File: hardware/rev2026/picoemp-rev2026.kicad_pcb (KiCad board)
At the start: 2 copper layers, 40 x 130 mm, 53 parts, among them J1 EDGE-SMA, J2 1x2_Pin_Header, J3 MKDS 1,5/2-5.08, J4 EDGE-SMA, P1 Header 7, P2 Header 2, P3 Header 4, Q1 LDA111STR, Q2 RGT16BM65DTL, Q3 AO3422, Q4 AO3422, SW1 KSC741J LFS, SW2 KSC741J LFS, SW3 TL3301AF160QJ, T1 ATB322524, T2 ATB322524, U1 SC0915, U2 74LVC1G17

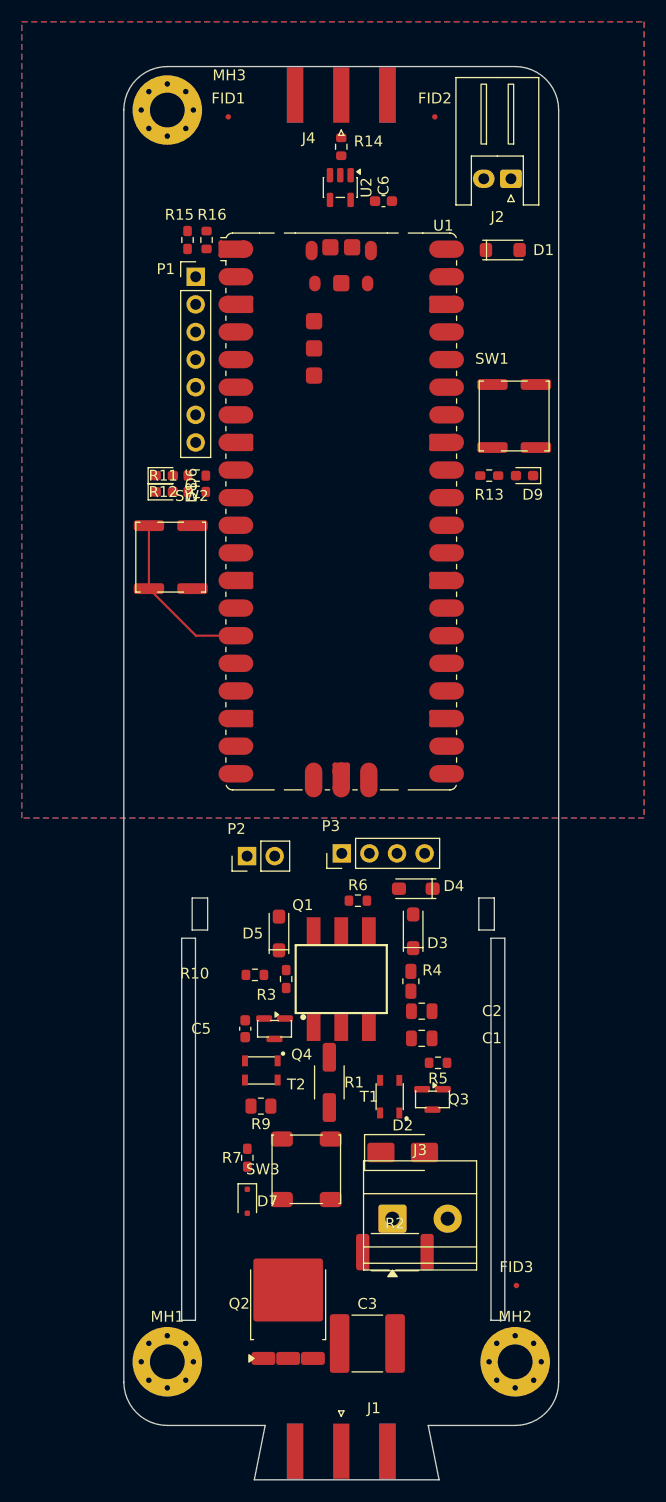
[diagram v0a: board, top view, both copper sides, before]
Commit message: Place fiducials clear of the HV section; J4 east-edge move blocked
Fiducials moved out of the old Altium scatter to three non-collinear spots,
all in the LOGIC half:
    FID1 (114.39, 23.872)   north-west
    FID2 (140.39, 41.000)   east, between D1 and SW1
    FID3 (108.39, 88.000)   west, below the Pico

None goes in the HV island or its side strips. A fiducial is unconnected
copper, and floating copper beside a 250 V section is exactly what was just
taken off the mounting holes in 0d4738f.

Worth stating plainly: with a hand build and no PCBA, these do nothing. They are
optical alignment targets for a pick-and-place machine. Placed as asked, but
deleting FID1-3 outright would be defensible.

J4 STAYS ON THE NORTH EDGE. The east-edge move was applied and then reverted:
Connector_Coaxial:SMA_Amphenol_132289_EdgeMount reports 4 shorting_items and
solder_mask_bridge violations between pad 1 (signal) and pad 2 (ground) at
rotations 0 and 180, and zero at 90 and -90. Measured across all four:

    rot    0 -> 4 violations
    rot   90 -> 0
    rot  180 -> 4
    rot  -90 -> 0

A rigid footprint cannot change whether its own pads overlap when you rotate it,
so one of the two readings is wrong. Rendering the footprint's F.Cu settles the
geometry: the three pads come out 5.080 x 1.500 mm on a 4.25 mm pitch, a clean
2.75 mm gap, no overlap. The pads are fine and the short is an artefact.

Which means the blocker is not the layout. But DRC is the fab gate, and shipping
the trigger connector in an orientation that trips a short I cannot account for
is worse than leaving it where it is. Note J1 -- the HV output SMA, on the same
footprint -- is at rot -90 and therefore in the clean set.

This also explains the pad-axis confusion behind the unresolved Q2 item: the
same (size a b) reading that makes these SMA pads overlap is what produces Q2's
0.080 mm. The two are one question, not two.

The USB collision is still real and unfixed: J4's courtyard spans x 118.81..129.97
on the no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
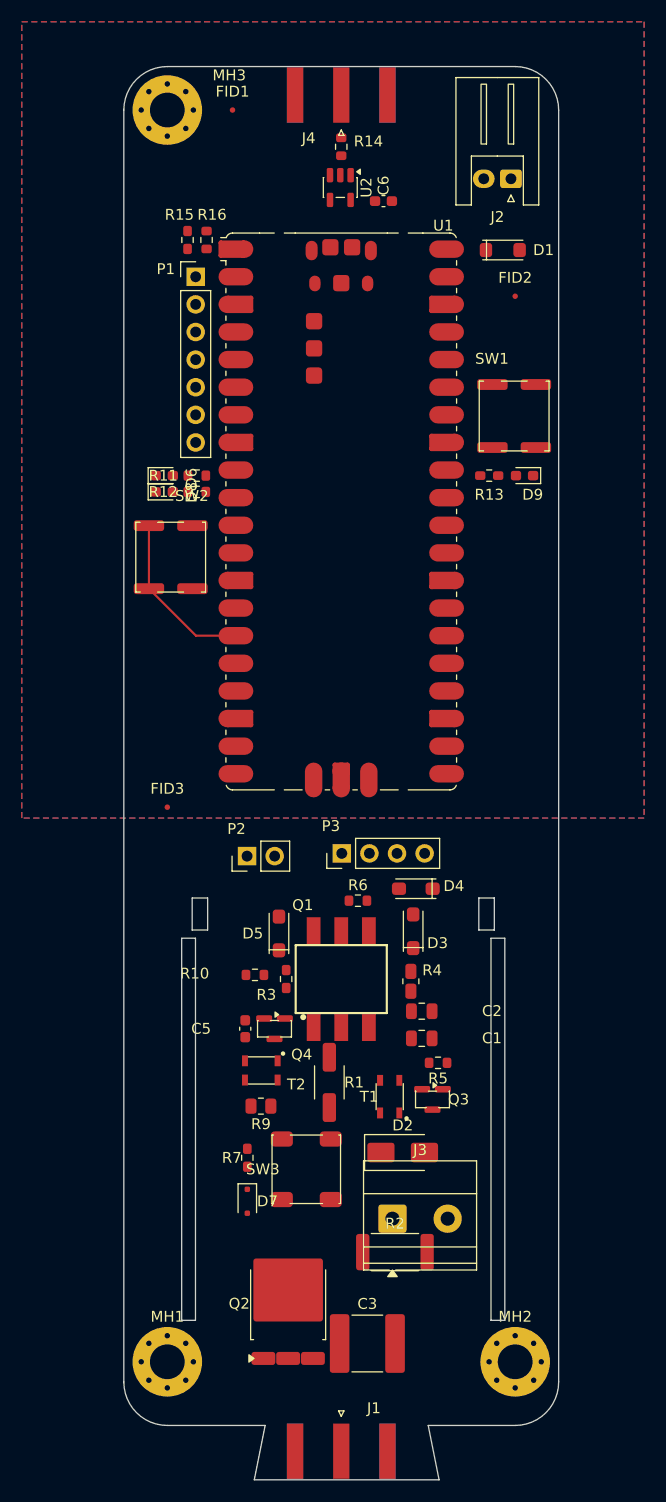
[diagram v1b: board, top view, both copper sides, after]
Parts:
- moved FID3 54.5 mm to (108.4, 88.0)
- moved FID2 18.1 mm to (140.4, 41.0)
- moved FID1 0.74 mm to (114.4, 23.9)
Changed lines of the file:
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@@
 	(footprint "Fiducial:Fiducial_0.5mm_Mask1.5mm"
 		(layer "F.Cu")
-		(at 140.5 132)
+		(at 108.39 88)
 		(descr "Fiducial, circular marking, 0.5mm bare copper, 1.5mm soldermask opening")
 		(tags "fiducial")
@@
 	(footprint "Fiducial:Fiducial_0.5mm_Mask1.5mm"
 		(layer "F.Cu")
-		(at 133 24.5)
+		(at 140.39 41)
 		(descr "Fiducial, circular marking, 0.5mm bare copper, 1.5mm soldermask opening")
 		(tags "fiducial")
@@
 	(footprint "Fiducial:Fiducial_0.5mm_Mask1.5mm"
 		(layer "F.Cu")
-		(at 114 24.5)
+		(at 114.39 23.872)
 		(descr "Fiducial, circular marking, 0.5mm bare copper, 1.5mm soldermask opening")
 		(tags "fiducial")

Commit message: Align MH1/MH2 with the bottom corners; correct the shield constraint claim
MH1/MH2 move 1.855 mm south to y=140.872, putting them 4.000 mm from the south
edge as well as 4.000 mm from the side edges. The R=4.000 corner arcs are
centred on exactly those points, so all three mounting holes now sit concentric
in their corners with a constant 2.400 mm FR4 web, instead of only MH3.

I previously said their Y was fixed by the Hammond 1551B shield and could not
move. That was inference from upstream's layout, not something I had checked,
and it was overstated. hardware/shield/picoempshield-1551BTRD-top.stl is
50 x 25 x 8 mm with corner bosses and contains no 32 mm screw pattern, so
nothing in the repo pins these holes to y=139.017.

What does matter is the 32.000 mm X spacing between MH1 and MH2 -- that is the
dimension a shield or bracket keys off. Only Y changed; a test now asserts the
spacing so a future corner tweak cannot quietly take it with it.

Since this rests on inference rather than a drawing, check the 1.855 mm shift
against the physical shield before ordering. If its screws are fixed relative to
the south edge, revert the Y and accept that the bottom corners are not
concentric.

Geometry checked: hole edges clear the shortened isolation slots by 4.07 mm and
the south board edge by 2.400 mm.

Test replaced with an all-holes version, plus the X-spacing guard: 68 -> 69.
DRC errors still 7, parity clean.

Co-Authored-By: Claude Opus 5 <noreply@anthropic.com>
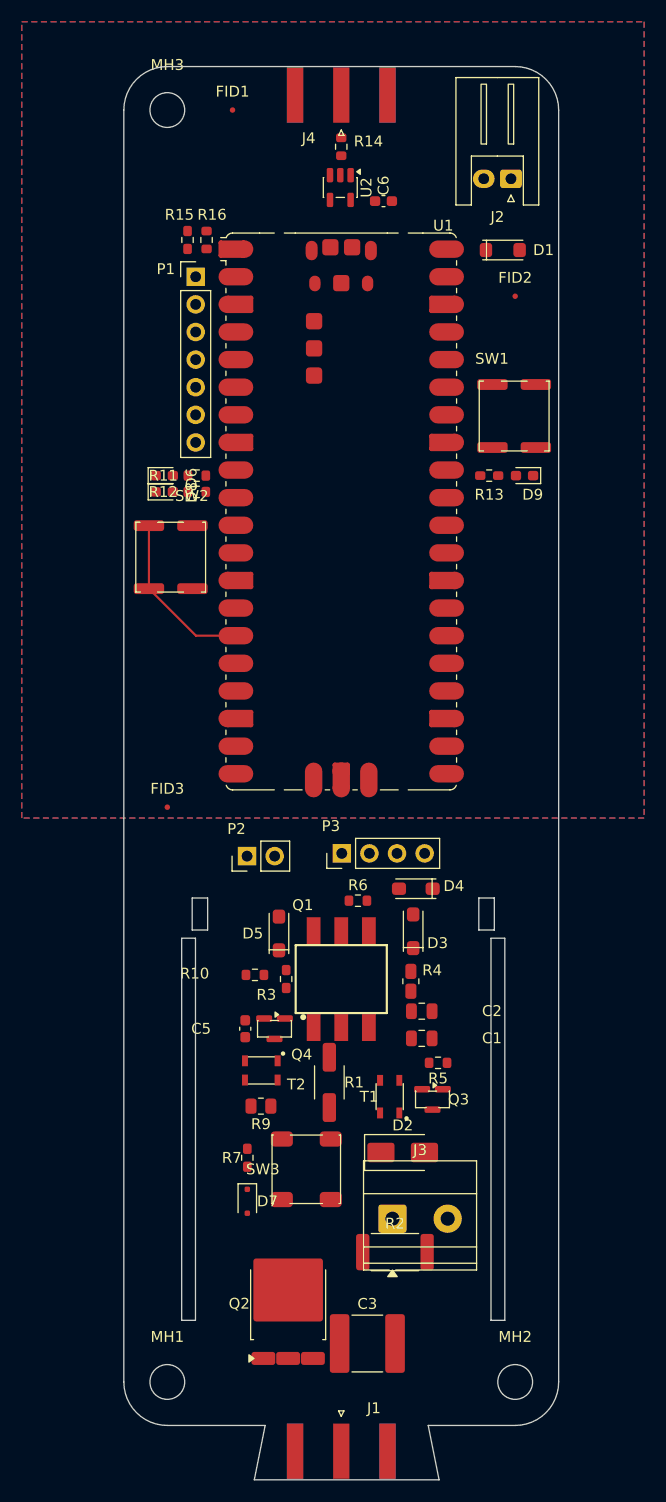
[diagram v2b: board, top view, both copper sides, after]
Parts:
- MH1, MH2, MH3: footprint MountingHole:MountingHole_3.2mm_M3_Pad_Via -> MountingHole:MountingHole_3.2mm_M3
- moved MH1 1.85 mm to (108.4, 140.9)
- moved MH2 1.85 mm to (140.4, 140.9)

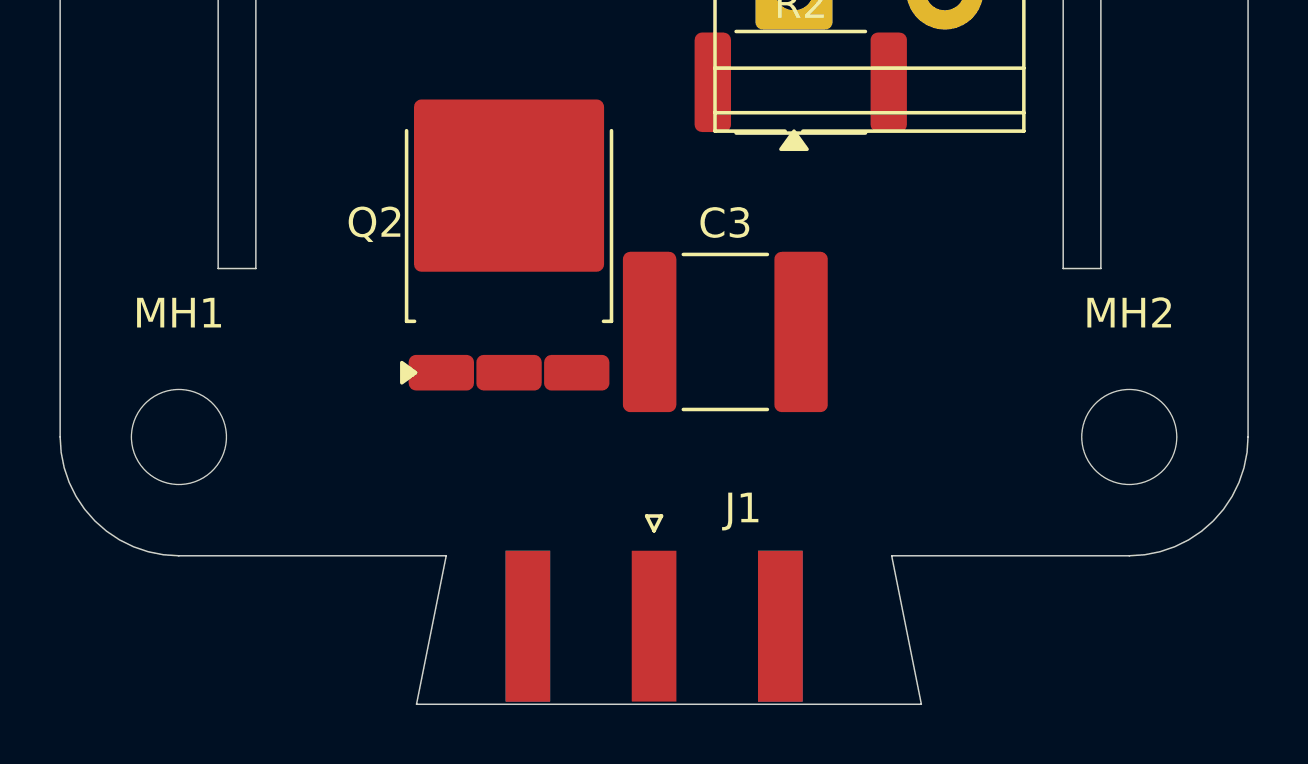
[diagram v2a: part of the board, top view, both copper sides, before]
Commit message: Centre the HV SMA tab; settle the pad-size axis question by plotting
The outcropping for J1 was drawn 0.500 mm east of the board centreline -- tab
centred on x=124.890 against a board centre of x=124.390. J1 itself sits at
x=124.390, so the connector was centred on the board but off-centre in its own
tab. Shifting the tab west by 0.500 mm centres both.

Separately, the pad-size axis question behind BOTH the Q2 0.080 mm item and the
J4 rotation short is now resolved, by plotting F.Cu and measuring the copper
that would actually reach the gerbers rather than reasoning about coordinates:

  J1 / J4 pads   1.500 mm wide, 4.250 mm pitch  -> 2.750 mm gaps.  Fine.
  Q2 lead pads   2.200 mm wide, 2.280 mm pitch  -> 0.080 mm gaps.  NOT fine.

So Q2's 0.080 mm is REAL, not a DRC artefact. The plot is the fabrication
output, and in it the three TO-252 lead pads are 2.200 mm across on a 2.286 mm
pitch. Those pads are HV_GATE, HV_OUT (collector) and HV_RTN (emitter). Holding
~250 V across 0.080 mm is close to the ~240 V that gap breaks down at in air,
and it is below JLCPCB's 0.127 mm minimum besides. Q2 needs a corrected
footprint before this board is ordered. Leaving the violation visible rather
than excluding it was the right call.

The same measurement explains J4: its pads only clear at rotations 90 and -90.
At 0 and 180 the plotted copper genuinely overlaps, so the east-edge placement
the user asked for cannot use this footprint as drawn. J1 is at -90 and is
clean.

Tests 69 -> 70.

Co-Authored-By: Claude Opus 5 <noreply@anthropic.com>
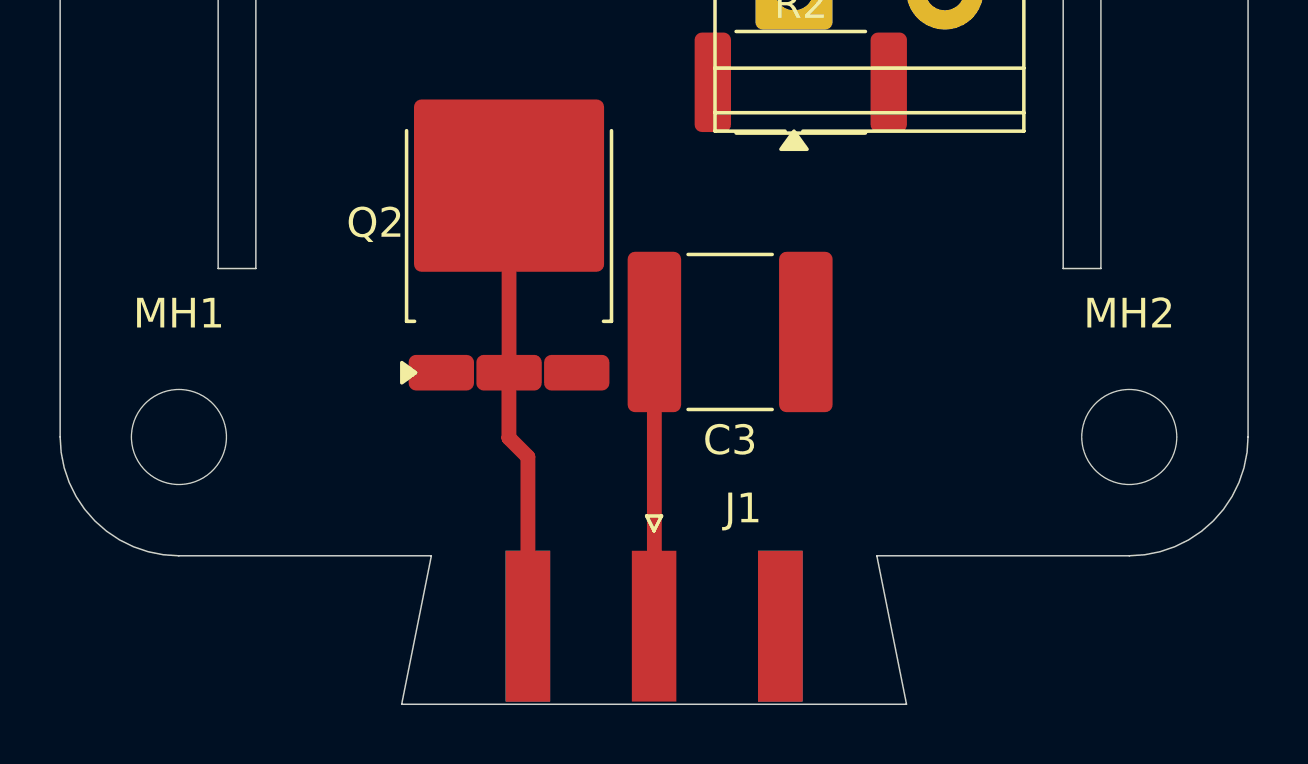
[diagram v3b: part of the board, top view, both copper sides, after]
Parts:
- moved C3 0.16 mm to (127.0, 137.3), turned to 180 degrees
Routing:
- net /HV_OUT: track 0.00 -> 16.0 mm
- net /HV_RAIL: track 0.00 -> 9.91 mm
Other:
- outline, holes or cut-outs redrawn
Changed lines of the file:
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@@
 	(footprint "Capacitor_SMD:C_2220_5750Metric"
 		(layer "F.Cu")
-		(at 126.7892 137.3357)
+		(at 126.95 137.3357 180)
 		(descr "Capacitor SMD 2220 (5750 Metric), square (rectangular) end terminal, IPC-7351 nominal, (Body size from: http://datasheets.avx.com/AVX-HV_MLCC.pdf)")
 		(tags "capacitor")
@@
 		)
 		(property "DigiKey" "490-16845-1-ND"
-			(at 0 0 0)
+			(at 0 0 180)
 			(unlocked yes)
 			(layer "F.Fab")
@@
 		)
 		(property "Manufacturer" "Murata"
-			(at 0 0 0)
+			(at 0 0 180)
 			(unlocked yes)
 			(layer "F.Fab")
@@
 		)
 		(property "MPN" "KRM55TR72J474MH01K"
-			(at 0 0 0)
+			(at 0 0 180)
 			(unlocked yes)
 			(layer "F.Fab")
@@
 		(duplicate_pad_numbers_are_jumpers no)
 		(fp_line
+			(start -1.415748 2.61)
+			(end 1.415748 2.61)
+			(stroke
+				(width 0.12)
+				(type solid)
+			)
+			(layer "F.SilkS")
+		)
+		(fp_line
 			(start -1.415748 -2.61)
 			(end 1.415748 -2.61)
-			(stroke
-				(width 0.12)
-				(type solid)
-			)
-			(layer "F.SilkS")
-		)
-		(fp_line
-			(start -1.415748 2.61)
-			(end 1.415748 2.61)
 			(stroke
 				(width 0.12)
@@
 		)
 		(pad "1" smd roundrect
-			(at -2.55 0)
+			(at -2.55 0 180)
 			(size 1.8 5.4)
 			(layers "F.Cu" "F.Mask" "F.Paste")
@@
 		)
 		(pad "2" smd roundrect
-			(at 2.55 0)
+			(at 2.55 0 180)
 			(size 1.8 5.4)
 			(layers "F.Cu" "F.Mask" "F.Paste")
@@
 	(gr_line
 		(start 108.39 144.872)
-		(end 117.39 144.872)
+		(end 116.89 144.872)
 		(stroke
 			(width 0.05)
@@
 	)
 	(gr_line
-		(start 116.39 149.872)
-		(end 133.39 149.872)
-		(stroke
-			(width 0.05)
-			(type solid)
-		)
-		(layer "Edge.Cuts")
-	)
-	(gr_line
-		(start 117.39 144.872)
-		(end 116.39 149.872)
-		(stroke
-			(width 0.05)
-			(type solid)
-		)
-		(layer "Edge.Cuts")
-	)
-	(gr_line
-		(start 132.39 144.872)
+		(start 115.89 149.872)
+		(end 132.89 149.872)
+		(stroke
+			(width 0.05)
+			(type solid)
+		)
+		(layer "Edge.Cuts")
+	)
+	(gr_line
+		(start 116.89 144.872)
+		(end 115.89 149.872)
+		(stroke
+			(width 0.05)
+			(type solid)
+		)
+		(layer "Edge.Cuts")
+	)
+	(gr_line
+		(start 131.89 144.872)
 		(end 140.39 144.872)
 		(stroke
@@
 	)
 	(gr_line
-		(start 133.39 149.872)
-		(end 132.39 144.872)
+		(start 132.89 149.872)
+		(end 131.89 144.872)
 		(stroke
 			(width 0.05)
@@
 	)
 	(segment
+		(start 124.4 137.3357)
+		(end 124.4 147.2317)
+		(width 0.5)
+		(layer "F.Cu")
+		(net "/HV_RAIL")
+	)
+	(segment
+		(start 124.4 147.2317)
+		(end 124.39 147.2417)
+		(width 0.5)
+		(layer "F.Cu")
+		(net "/HV_RAIL")
+	)
+	(segment
+		(start 119.8 139.0021)
+		(end 119.5054 138.7075)
+		(width 0.5)
+		(layer "F.Cu")
+		(net "/HV_OUT")
+	)
+	(segment
+		(start 119.5 140.9021)
+		(end 120.14 141.5421)
+		(width 0.5)
+		(layer "F.Cu")
+		(net "/HV_OUT")
+	)
+	(segment
+		(start 120.14 141.5421)
+		(end 120.14 147.2417)
+		(width 0.5)
+		(layer "F.Cu")
+		(net "/HV_OUT")
+	)
+	(segment
+		(start 119.5 138.7129)
+		(end 119.5 140.9021)
+		(width 0.5)
+		(layer "F.Cu")
+		(net "/HV_OUT")
+	)
+	(segment
+		(start 119.5054 132.4075)
+		(end 119.5054 138.7075)
+		(width 0.5)
+		(layer "F.Cu")
+		(net "/HV_OUT")
+	)
+	(segment
+		(start 120.14 147.2417)
+		(end 119.8 146.9017)
+		(width 0.5)
+		(layer "F.Cu")
+		(net "/HV_OUT")
+	)
+	(segment
+		(start 119.5054 138.7075)
+		(end 119.5 138.7129)
+		(width 0.5)
+		(layer "F.Cu")
+		(net "/HV_OUT")
+	)
+	(segment
